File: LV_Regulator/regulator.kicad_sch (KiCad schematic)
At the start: 47 parts, among them U5 BQ25858QWRRVRQ1, U6 CSD19506KTT, U7 CSD19506KTT, U8 CSD19506KTT, U9 CSD19506KTT

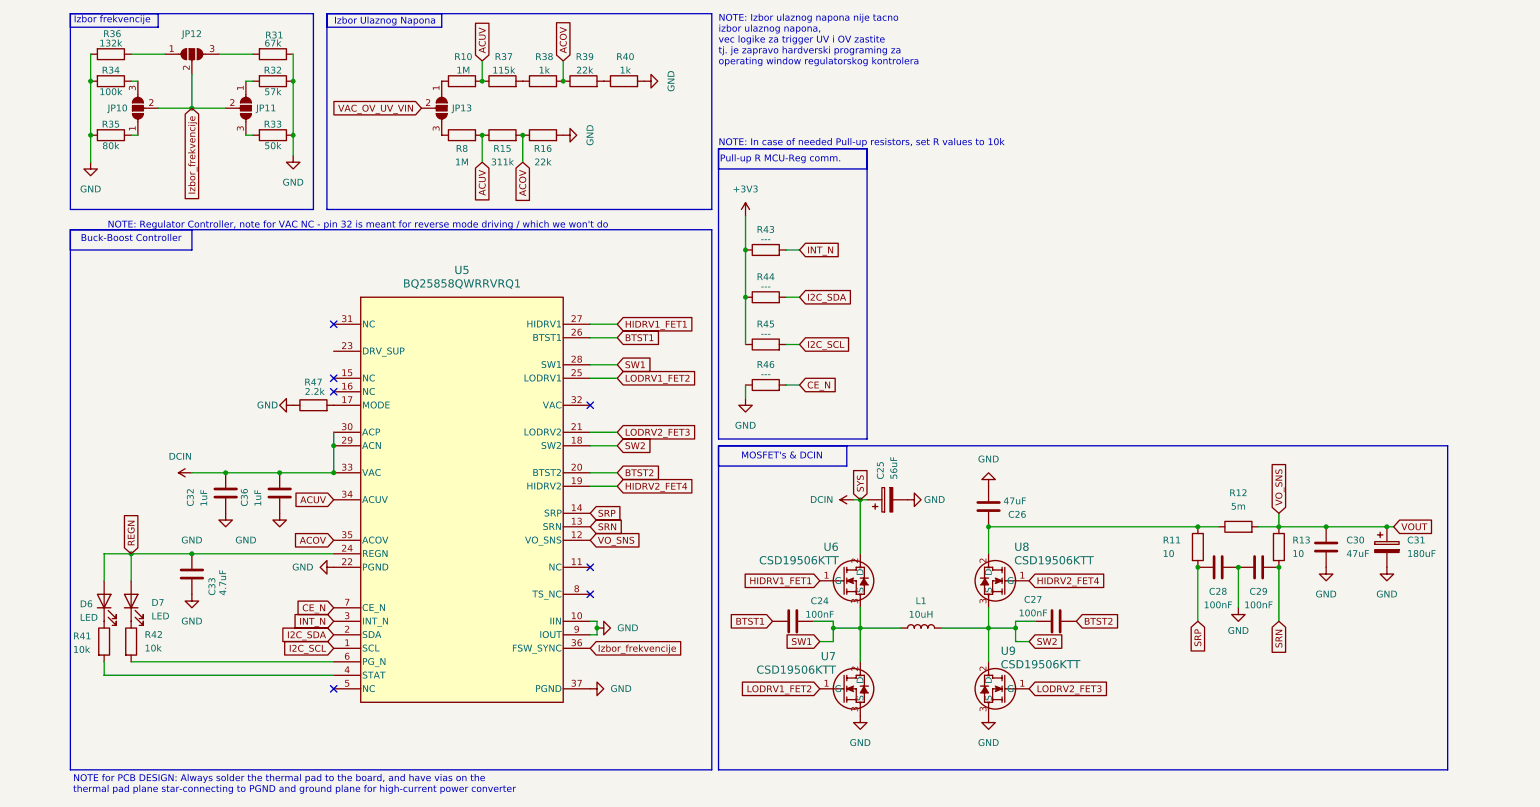
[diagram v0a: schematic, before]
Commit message: Added Footprints & Links for Component Purchase
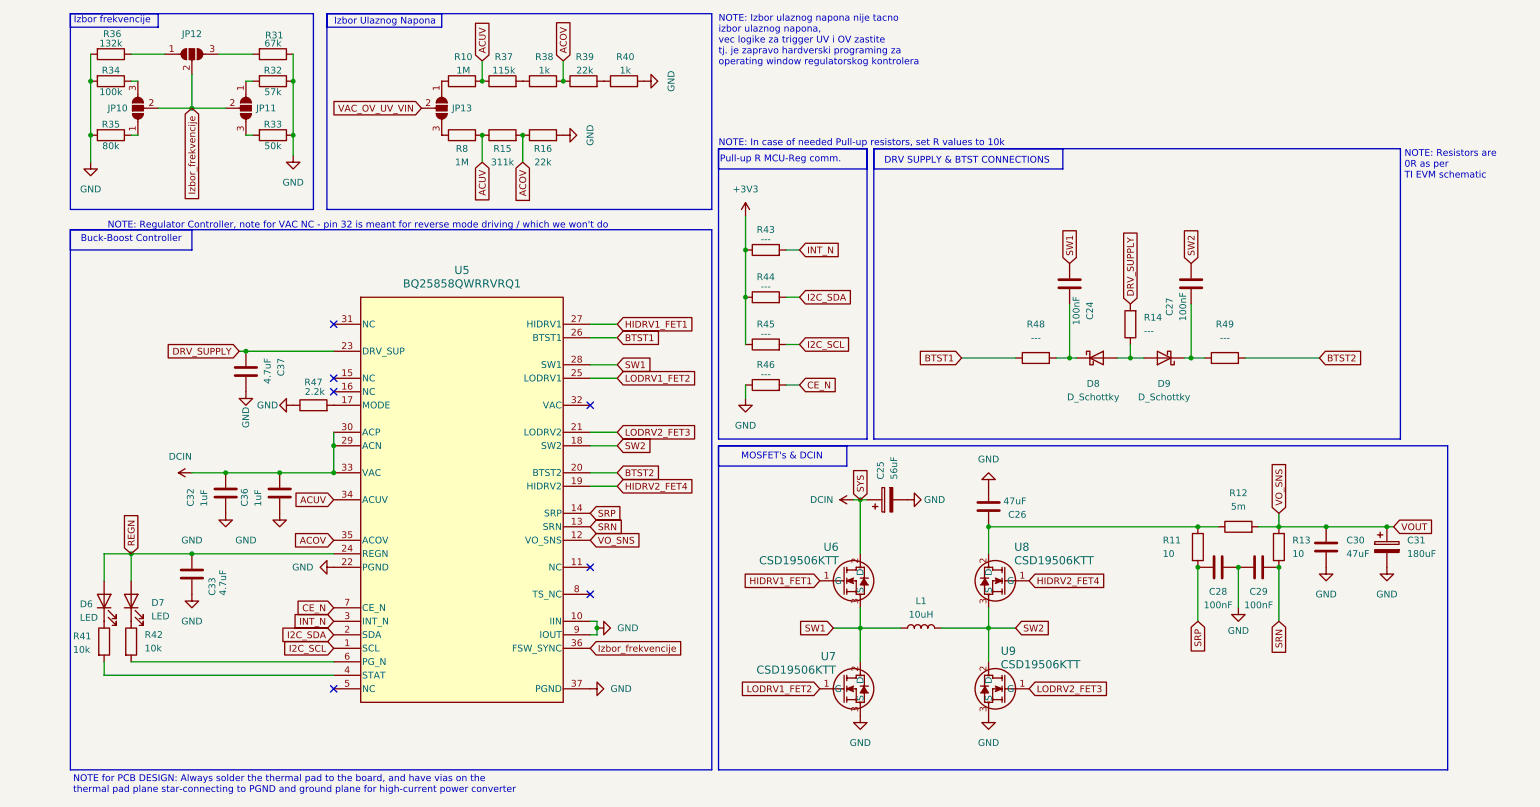
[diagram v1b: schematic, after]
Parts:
- added C37: 4.7uF, Capacitor_SMD:C_1206_3216Metric, symbol Device:C
- added D8, D9: D_Schottky, V1FM10-M3/H:SODFL3718X108N, symbol Device:D_Schottky
- added R14, R48, R49: ---, Resistor_SMD:R_1206_3216Metric_Pad1.30x1.75mm_HandSolder, symbol Device:R
- C27: Purchase Place https://www.digikey.com/en/products/detail/kemet/C1206C104K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 -> https://eu.mouser.com/ProductDetail/KEMET/C1206C104K3RAC741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
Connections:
- net BTST1: now also R48.1; no longer C24.1
- net BTST2: now also R49.2; no longer C27.1
- net GND: now also C37.2
- net SW1: now also C24.1; no longer C24.2
- net SW2: now also C27.1; no longer C27.2
- net DRV_SUPPLY: now reaches U5.23 (DRV_SUP)
- net DRV_SUPPLY: now also C37.1, R14.2
- new net: C27.2, D9.1 (K), R49.1
- new net: C24.2, D8.1 (K), R48.2
- new net: D8.2 (A), D9.2 (A), R14.1
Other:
- note added: "DRV SUPPLY & BTST CONNECTIONS"
- note added: "NOTE: Resistors are 0R as per TI EVM schematic"
- moved on the sheet: C24, C27

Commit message: Halfway Push of adding 3D models to PCB layout components
Pushing with components left to add to finish on main PC
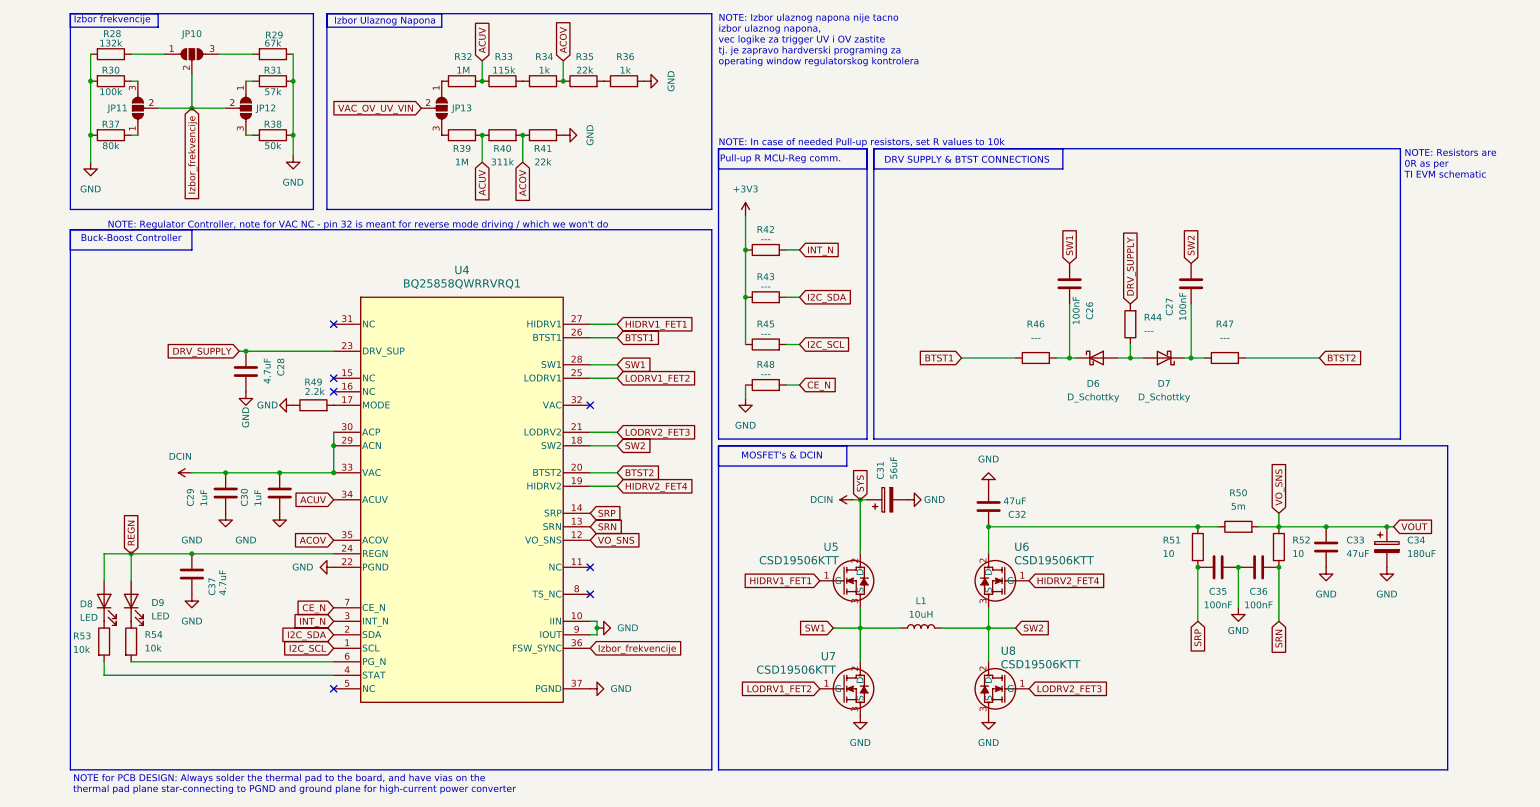
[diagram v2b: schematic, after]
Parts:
- renumbered C24 to C26, C37 to C28, C32 to C29, C36 to C30, C25 to C31, C26 to C32, C30 to C33, C31 to C34, C28 to C35, C29 to C36, C33 to C37, D8 to D6, D9 to D7, D6 to D8, D7 to D9, JP12 to JP10, JP10 to JP11, JP11 to JP12, R36 to R28, R31 to R29, R34 to R30, R32 to R31, R10 to R32, R37 to R33, R38 to R34, R39 to R35, R40 to R36, R35 to R37, R33 to R38, R8 to R39, R15 to R40, R16 to R41, R43 to R42, R44 to R43, R14 to R44, R48 to R46, R49 to R47, R46 to R48, R47 to R49, R12 to R50, R11 to R51, R13 to R52, R41 to R53, R42 to R54, U5 to U4, U6 to U5, U8 to U6, U9 to U8

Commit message: LV Regulator Switching layout Started
Rough placement of components bigger components, a well as giving a capacitor a 3D model it lacked for the 3D View.
More precise placement is in queue and actual PCB routing.
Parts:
- JP12: footprint Jumper:SolderJumper-3_P1.3mm_Open_Pad1.0x1.5mm -> Jumper:SolderJumper-3_P1.3mm_Open_RoundedPad1.0x1.5mm
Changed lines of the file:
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@@
 			)
 		)
-		(property "Footprint" "Jumper:SolderJumper-3_P1.3mm_Open_Pad1.0x1.5mm"
+		(property "Footprint" "Jumper:SolderJumper-3_P1.3mm_Open_RoundedPad1.0x1.5mm"
 			(at 45.72 30.48 0)
 			(effects

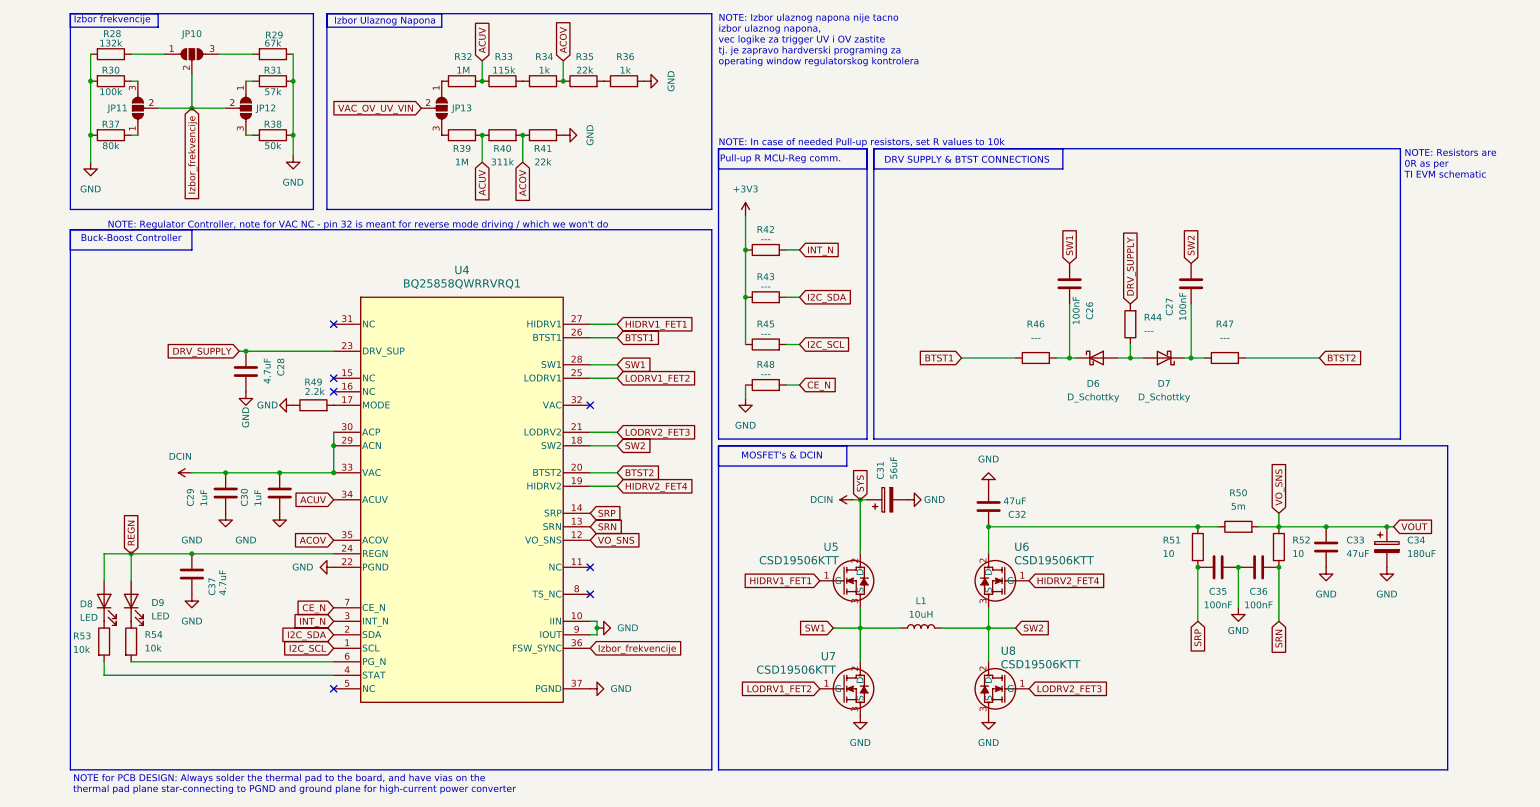
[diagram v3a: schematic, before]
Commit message: Multiple Fixes in Schematic & Routing
Fixed multiple issues in schematic, like adding jumpers to isolate ACUV/ACOV between the choices. Moved the fuses on the Logic_Supply as per instruction of professor from Chair of Electronics, FoTS, UoNS. Started and made good progress on Power Electronics (Regulator Side) of the PCB.
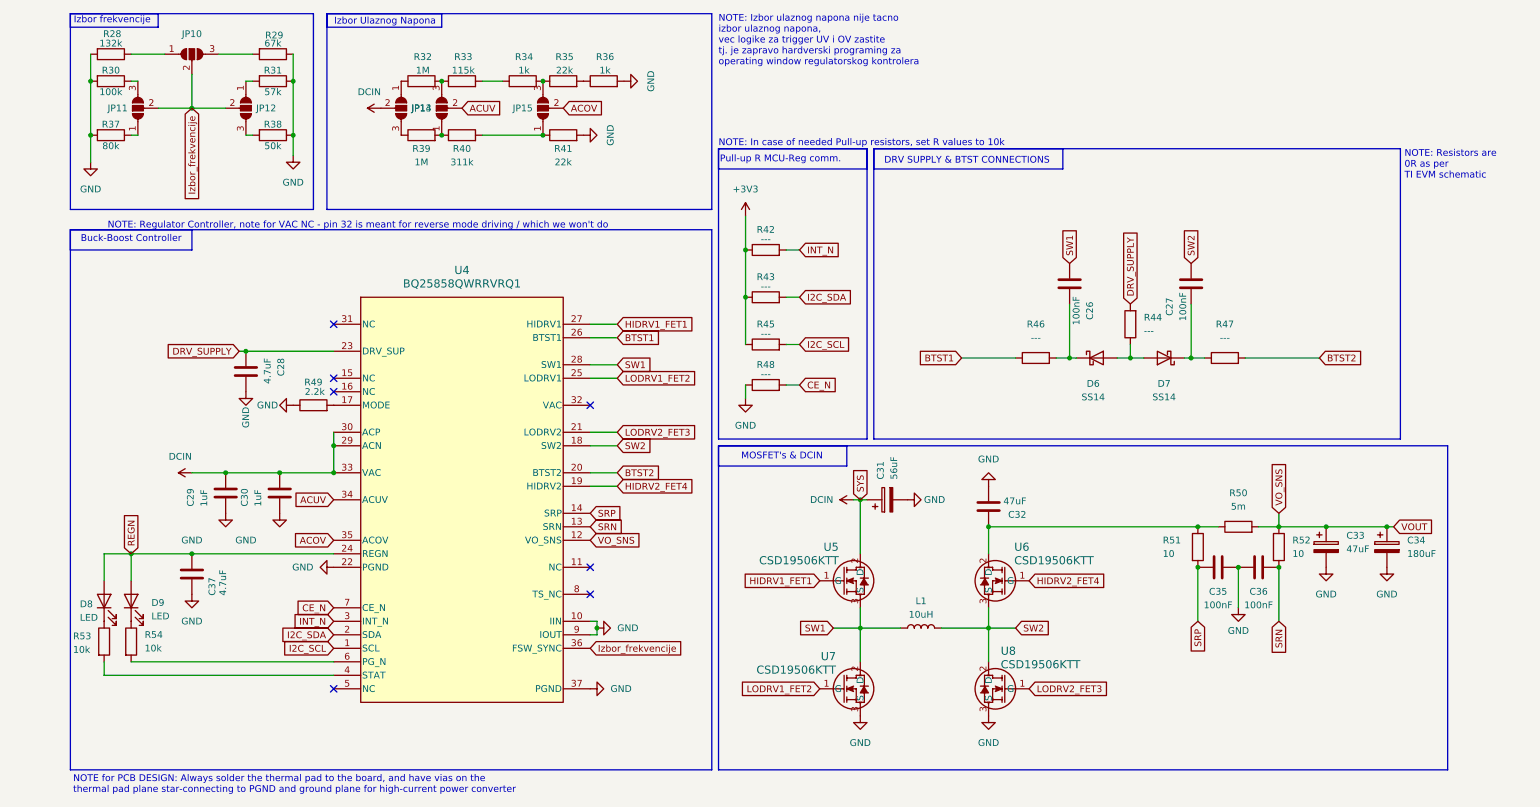
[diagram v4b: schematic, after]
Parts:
- added JP14, JP15: SolderJumper_3_Open, Jumper:SolderJumper-3_P1.3mm_Open_RoundedPad1.0x1.5mm, symbol Jumper:SolderJumper_3_Open
- C33: symbol Device:C -> Device:C_Polarized
- D6, D7: value D_Schottky -> SS14; footprint V1FM10-M3/H:SODFL3718X108N -> SS14:CR_SMA_403AE_OSI; Purchase Place https://eu.mouser.com/ProductDetail/Vishay-General-Semicond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 -> https://www.digikey.com/en/products/detail/onsemi/ss14/9654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
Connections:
- net VAC_OV_UV_VIN is gone; now on net DCIN: JP13.2 (C)
- net ACOV: now also JP15.2 (C); no longer R34.2, R35.1, R40.2, R41.1
- net ACUV: now also JP14.2 (C); no longer R32.2, R33.1, R39.2, R40.1
- new net: JP15.3 (B), R34.2, R35.1
- new net: JP14.1 (A), R39.2, R40.1
- new net: JP14.3 (B), R32.2, R33.1
- new net: JP15.1 (A), R40.2, R41.1
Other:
- moved on the sheet: JP13, R32, R33, R34, R35, R36, R39, R40, R41
